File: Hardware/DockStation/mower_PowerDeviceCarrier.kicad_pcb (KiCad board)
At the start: 2 copper layers, 135.1 x 68.4 mm, 7 parts, among them J1 Conn_01x04, J2 Conn_01x04

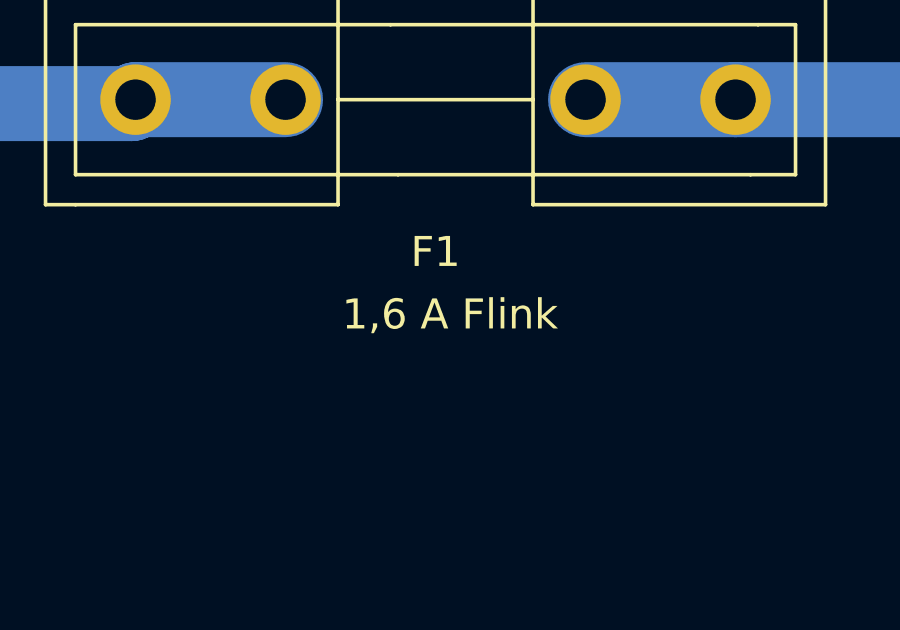
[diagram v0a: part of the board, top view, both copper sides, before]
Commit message: chore(dock): de translations
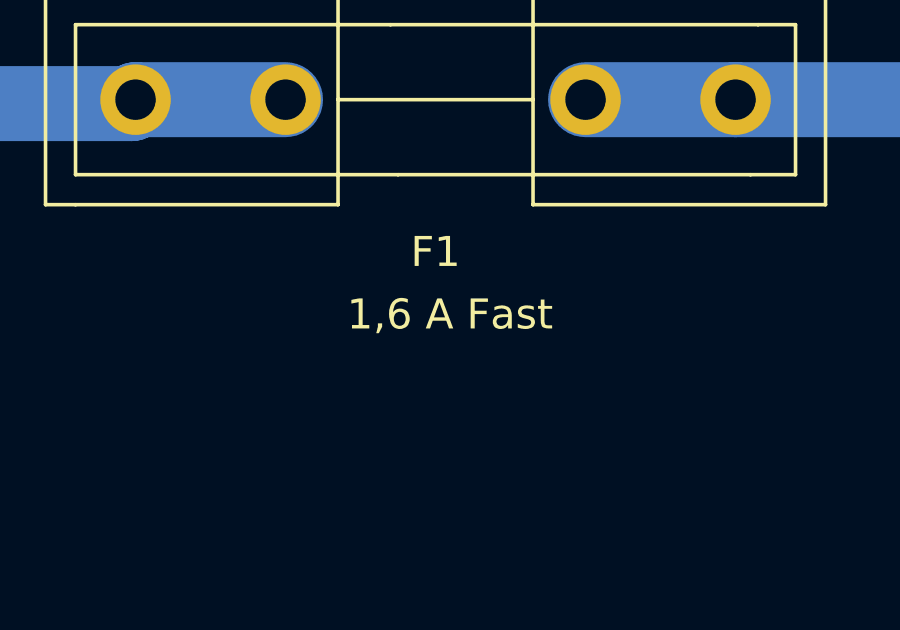
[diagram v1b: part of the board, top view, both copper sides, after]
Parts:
- A1: value DC-DC-Wandler -> DC-DC-Converter
- F1: value 1,6 A Flink -> 1,6 A Fast
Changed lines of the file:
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@@
       (effects (font (size 1 1) (thickness 0.15)))
     )
-    (fp_text value "1,6 A Flink" (at 9.5178 -7.1628) (layer "F.SilkS")
+    (fp_text value "1,6 A Fast" (at 9.5178 -7.1628) (layer "F.SilkS")
       (effects (font (size 1 1) (thickness 0.15)))
     )
@@
       (effects (font (size 1 1) (thickness 0.15)))
     )
-    (fp_text value "DC-DC-Wandler" (at 13.57 -1.76) (layer "F.Fab")
+    (fp_text value "DC-DC-Converter" (at 13.57 -1.76) (layer "F.Fab")
       (effects (font (size 1 1) (thickness 0.15)))
     )

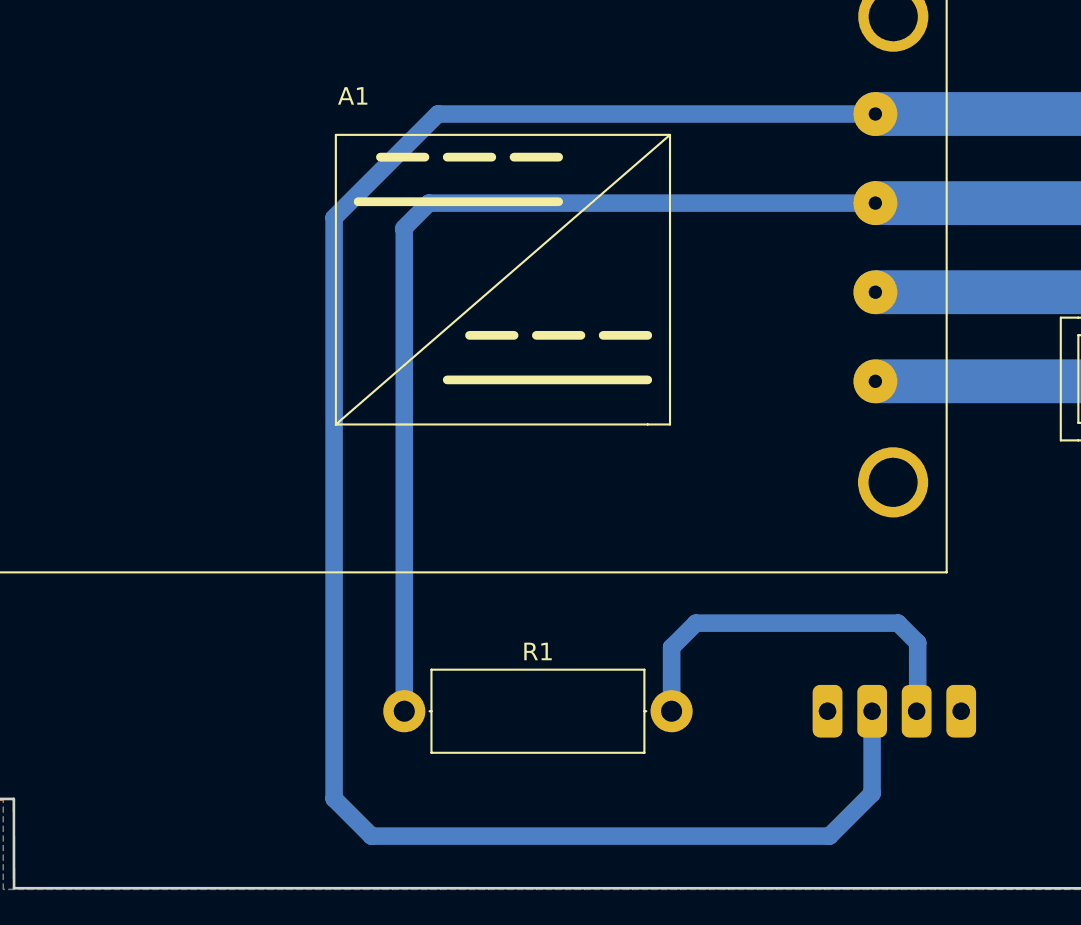
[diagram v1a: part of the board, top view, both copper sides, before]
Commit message: fix(dock): move led pin header to avoid screw hole overlap
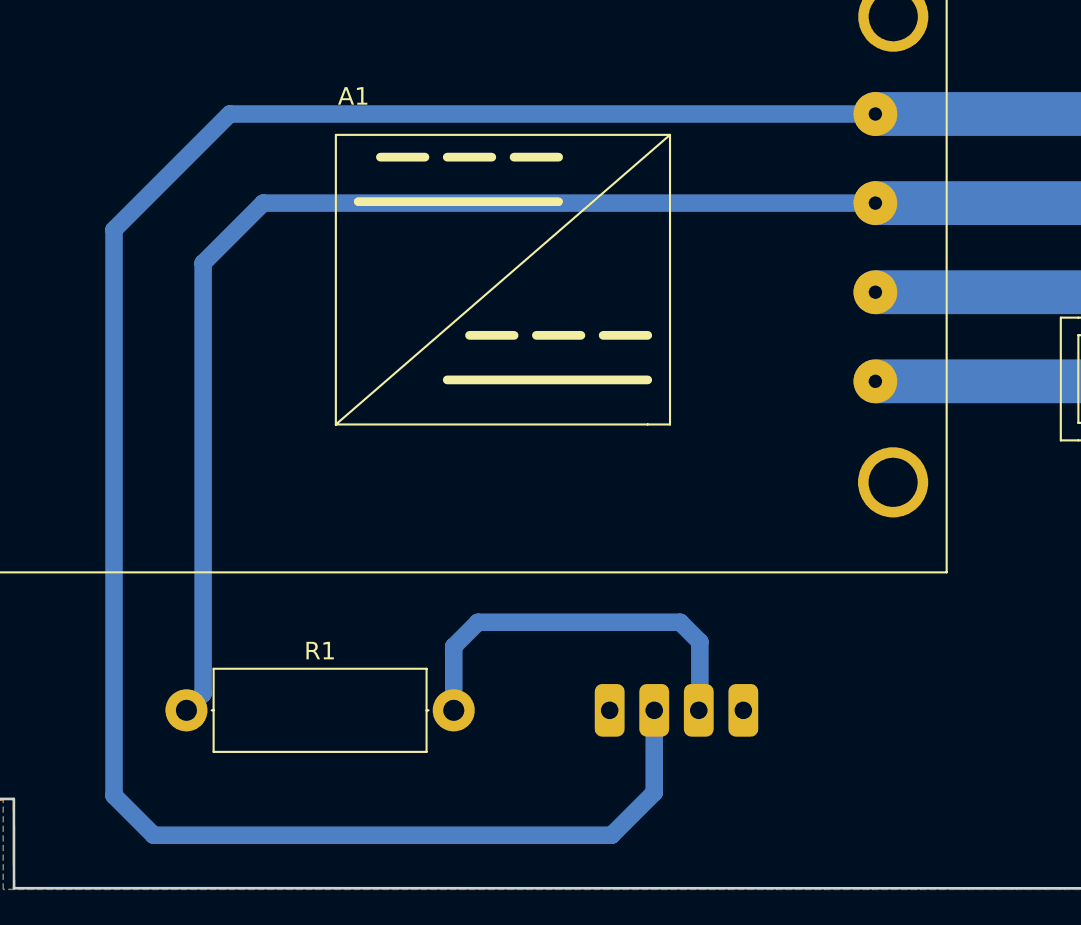
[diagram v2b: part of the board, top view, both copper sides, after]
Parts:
- moved R1 12.4 mm to (61.0, 109.3)
- moved J2 12.4 mm to (92.8, 109.3)
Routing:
- net +BATT: track 150.8 -> 162.9 mm
- net GND1: track 102.0 -> 112.7 mm
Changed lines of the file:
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@@
   )
   (footprint "Resistor_THT:R_Axial_DIN0414_L11.9mm_D4.5mm_P15.24mm_Horizontal" (layer "F.Cu")
-    (at 73.44 109.36)
+    (at 61.0194 109.3092)
     (descr "Resistor, Axial_DIN0414 series, Axial, Horizontal, pin pitch=15.24mm, 2W, length*diameter=11.9*4.5mm^2, http://www.vishay.com/docs/20128/wkxwrx.pdf")
     (tags "Resistor Axial_DIN0414 series Axial Horizontal pin pitch 15.24mm 2W length 11.9mm diameter 4.5mm")
@@
   )
   (footprint "ene9ba_footprint:PinHeader_1x04_P2.54mm_Horizontal" (layer "B.Cu")
-    (at 105.19 109.36 90)
+    (at 92.7694 109.3092 90)
     (descr "Through hole angled pin header, 1x04, 2.54mm pitch, 6mm pin length, single row")
     (tags "Through hole angled pin header THT 1x04 2.54mm single row")
@@
     (effects (font (size 1.5 1.5) (thickness 0.2)))
   )
-  (segment (start 74.844 80.3908) (end 73.4 81.8348) (width 1) (layer "B.Cu") (net 1))
-  (segment (start 100.2992 80.3908) (end 74.844 80.3908) (width 1) (layer "B.Cu") (net 1))
+  (segment (start 61.97 83.816) (end 65.3952 80.3908) (width 1) (layer "B.Cu") (net 1))
+  (segment (start 61.97 108.3586) (end 61.97 83.816) (width 1) (layer "B.Cu") (net 1))
   (segment (start 147.3427 80.3908) (end 147.3535 80.4016) (width 1) (layer "B.Cu") (net 1))
+  (segment (start 65.3952 80.3908) (end 100.2992 80.3908) (width 1) (layer "B.Cu") (net 1))
+  (segment (start 61.0194 109.3092) (end 61.97 108.3586) (width 1) (layer "B.Cu") (net 1))
   (segment (start 100.2992 80.3908) (end 147.3427 80.3908) (width 2.5) (layer "B.Cu") (net 1))
-  (segment (start 73.44 81.8748) (end 73.44 109.36) (width 1) (layer "B.Cu") (net 1))
+  (segment (start 85.2618 116.4296) (end 59.1506 116.4296) (width 1) (layer "B.Cu") (net 2))
+  (segment (start 87.6894 109.3092) (end 87.6894 114.002) (width 1) (layer "B.Cu") (net 2))
   (segment (start 100.2992 75.3108) (end 147.2627 75.3108) (width 2.5) (layer "B.Cu") (net 2))
-  (segment (start 100.11 109.36) (end 100.11 114.0528) (width 1) (layer "B.Cu") (net 2))
-  (segment (start 100.11 114.0528) (end 97.6824 116.4804) (width 1) (layer "B.Cu") (net 2))
-  (segment (start 69.4376 114.3468) (end 69.4376 81.2252) (width 1) (layer "B.Cu") (net 2))
-  (segment (start 97.6824 116.4804) (end 71.5712 116.4804) (width 1) (layer "B.Cu") (net 2))
+  (segment (start 87.6894 114.002) (end 85.2618 116.4296) (width 1) (layer "B.Cu") (net 2))
+  (segment (start 59.1506 116.4296) (end 56.89 114.169) (width 1) (layer "B.Cu") (net 2))
+  (segment (start 56.89 81.911) (end 63.4902 75.3108) (width 1) (layer "B.Cu") (net 2))
   (segment (start 147.2627 75.3108) (end 147.3535 75.4016) (width 1) (layer "B.Cu") (net 2))
-  (segment (start 75.352 75.3108) (end 100.2992 75.3108) (width 1) (layer "B.Cu") (net 2))
-  (segment (start 69.4376 81.2252) (end 75.352 75.3108) (width 1) (layer "B.Cu") (net 2))
-  (segment (start 71.5712 116.4804) (end 69.4376 114.3468) (width 1) (layer "B.Cu") (net 2))
+  (segment (start 63.4902 75.3108) (end 100.2992 75.3108) (width 1) (layer "B.Cu") (net 2))
+  (segment (start 56.89 114.169) (end 56.89 81.911) (width 1) (layer "B.Cu") (net 2))
   (segment (start 128.8702 90.42) (end 133.8702 90.42) (width 2.5) (layer "B.Cu") (net 5))
   (segment (start 133.8702 90.42) (end 147.3351 90.42) (width 2.5) (layer "B.Cu") (net 5))
@@
   (segment (start 100.2992 90.5508) (end 113.7394 90.5508) (width 2.5) (layer "B.Cu") (net 6))
   (segment (start 100.2992 85.4708) (end 147.2843 85.4708) (width 2.5) (layer "B.Cu") (net 7))
-  (segment (start 102.7116 109.2984) (end 102.65 109.36) (width 1) (layer "B.Cu") (net 8))
-  (segment (start 101.594 104.3392) (end 102.7116 105.4568) (width 1) (layer "B.Cu") (net 8))
-  (segment (start 102.7116 105.4568) (end 102.7116 109.2984) (width 1) (layer "B.Cu") (net 8))
-  (segment (start 88.68 109.36) (end 88.68 105.7216) (width 1) (layer "B.Cu") (net 8))
-  (segment (start 88.68 105.7216) (end 90.0624 104.3392) (width 1) (layer "B.Cu") (net 8))
-  (segment (start 90.0624 104.3392) (end 101.594 104.3392) (width 1) (layer "B.Cu") (net 8))
+  (segment (start 90.291 109.2476) (end 90.2294 109.3092) (width 1) (layer "B.Cu") (net 8))
+  (segment (start 89.1734 104.2884) (end 90.291 105.406) (width 1) (layer "B.Cu") (net 8))
+  (segment (start 90.291 105.406) (end 90.291 109.2476) (width 1) (layer "B.Cu") (net 8))
+  (segment (start 76.2594 109.3092) (end 76.2594 105.6708) (width 1) (layer "B.Cu") (net 8))
+  (segment (start 76.2594 105.6708) (end 77.6418 104.2884) (width 1) (layer "B.Cu") (net 8))
+  (segment (start 77.6418 104.2884) (end 89.1734 104.2884) (width 1) (layer "B.Cu") (net 8))
   (zone (net 7) (net_name "Net-(A1-Pad2)") (layers F&B.Cu) (hatch edge 0.508)
     (connect_pads (clearance 0.508))

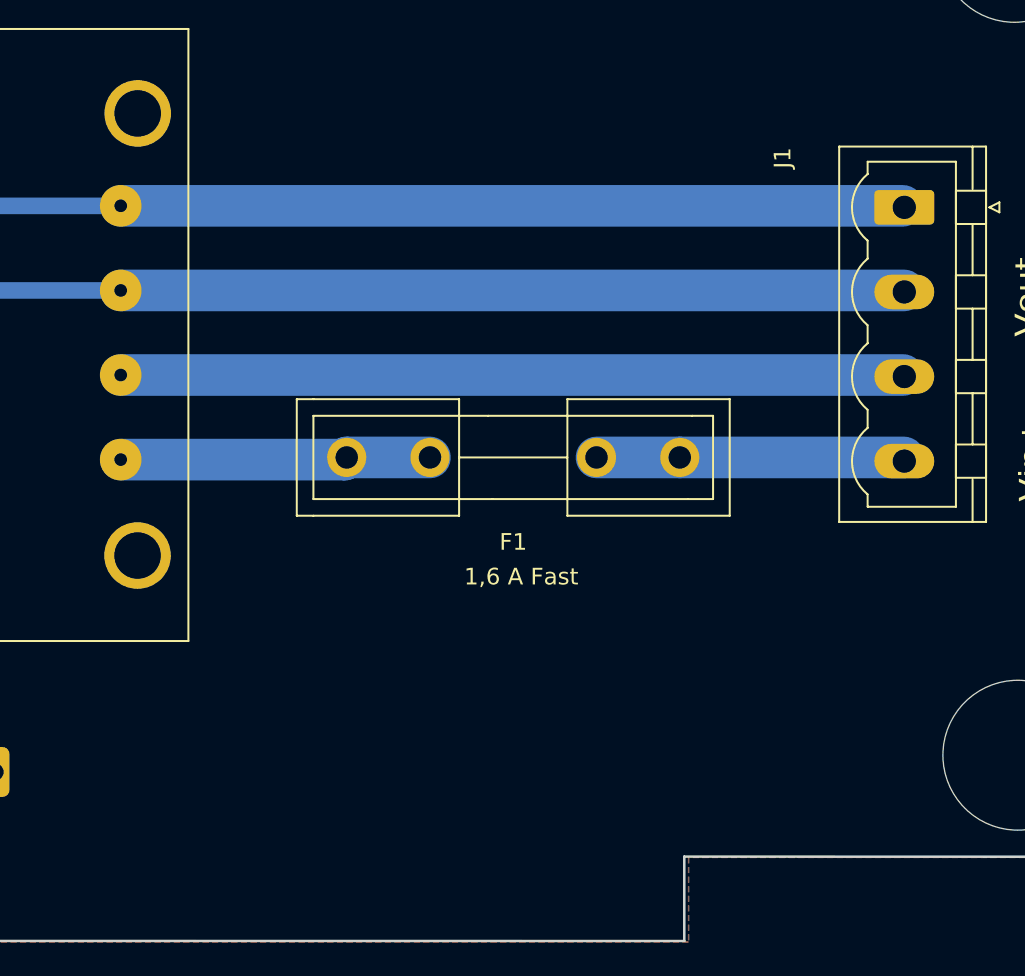
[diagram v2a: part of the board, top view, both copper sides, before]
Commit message: feat(dock): add 3.81mm terminals and pinholes to connect to dc/dc terminal
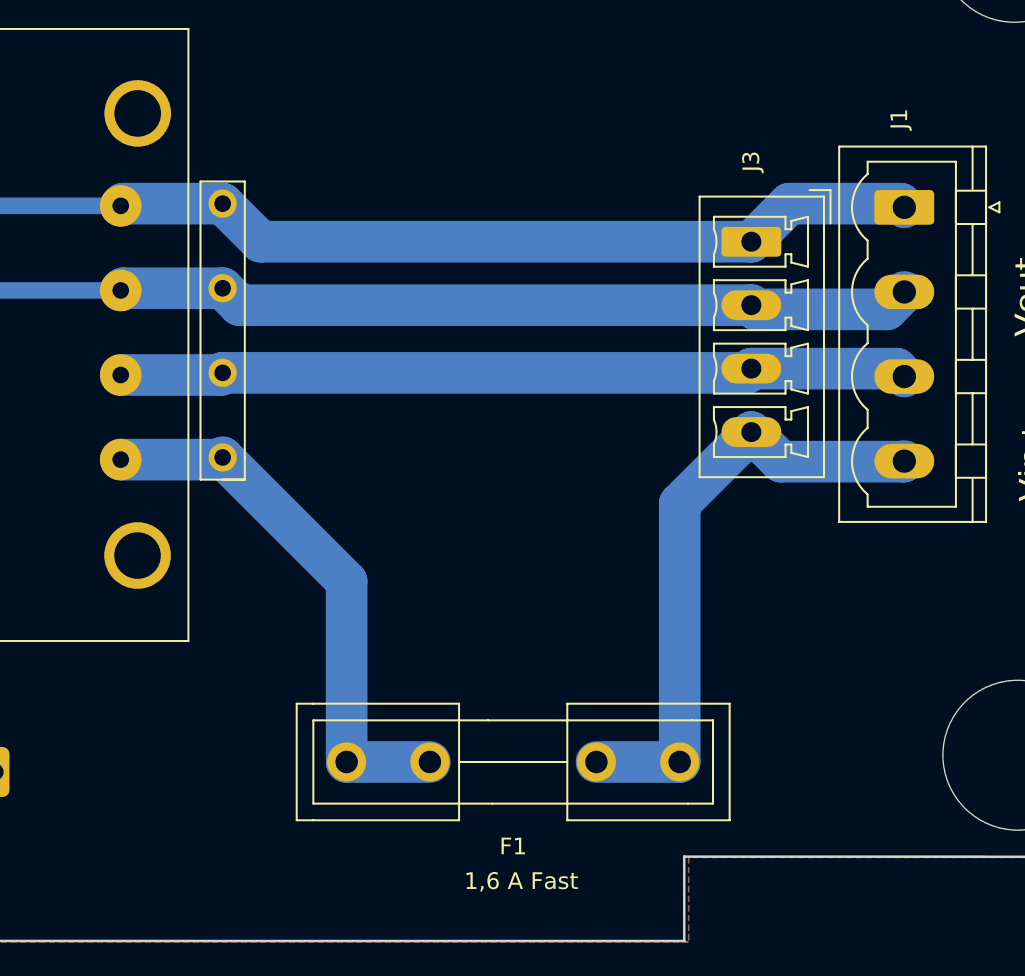
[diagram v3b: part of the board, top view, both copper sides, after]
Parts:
- removed REF**: ESD-Logo_6.6x6mm_SilkScreen, Symbol:ESD-Logo_6.6x6mm_SilkScreen
- added J3: Conn_01x04, Connector_Phoenix_MC:PhoenixContact_MCV_1,5_4-G-3.81_1x04_P3.81mm_Vertical, F.Cu at (138.2, 77.5)
- added J4: Conn_01x04, Connector_PinHeader_2.54mm:PinHeader_1x07_P2.54mm_Vertical, F.Cu at (106.4, 90.4)
- moved F1 18.3 mm to (133.9, 108.7)
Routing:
- net Net-(F1-Pad1): track 18.5 -> 36.5 mm
- net Net-(A1-Pad1): track 18.6 -> 32.5 mm
- net +BATT: track 162.9 -> 165.1 mm
- net GND1: track 112.7 -> 113.7 mm

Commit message: fix(dock): erc/drc
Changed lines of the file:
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@@
     (effects (font (size 1.5 1.5) (thickness 0.2)))
   )
+  (segment (start 147.3535 80.4816) (end 146.3051 81.53) (width 2.5) (layer "B.Cu") (net 1))
+  (segment (start 146.3051 81.53) (end 138.424 81.53) (width 2.5) (layer "B.Cu") (net 1))
   (segment (start 138.17 81.276) (end 107.436 81.276) (width 2.5) (layer "B.Cu") (net 1))
   (segment (start 138.17 81.276) (end 138.424 81.53) (width 2.5) (layer "B.Cu") (net 1))
   (segment (start 61.97 83.816) (end 65.3952 80.3908) (width 1) (layer "B.Cu") (net 1))
   (segment (start 61.97 108.3586) (end 61.97 83.816) (width 1) (layer "B.Cu") (net 1))
-  (segment (start 147.3427 80.3908) (end 147.3535 80.4016) (width 1) (layer "B.Cu") (net 1))
   (segment (start 106.42 80.26) (end 100.43 80.26) (width 2.5) (layer "B.Cu") (net 1))
-  (segment (start 138.424 81.53) (end 146.3051 81.53) (width 2.5) (layer "B.Cu") (net 1))
   (segment (start 65.3952 80.3908) (end 100.2992 80.3908) (width 1) (layer "B.Cu") (net 1))
   (segment (start 107.436 81.276) (end 106.42 80.26) (width 2.5) (layer "B.Cu") (net 1))
   (segment (start 61.0194 109.3092) (end 61.97 108.3586) (width 1) (layer "B.Cu") (net 1))
   (segment (start 100.43 80.26) (end 100.2992 80.3908) (width 2.5) (layer "B.Cu") (net 1))
-  (segment (start 146.3051 81.53) (end 147.3535 80.4816) (width 2.5) (layer "B.Cu") (net 1))
   (segment (start 85.2618 116.4296) (end 59.1506 116.4296) (width 1) (layer "B.Cu") (net 2))
   (segment (start 87.6894 109.3092) (end 87.6894 114.002) (width 1) (layer "B.Cu") (net 2))
@@
   (segment (start 100.43 75.18) (end 100.2992 75.3108) (width 2.5) (layer "B.Cu") (net 2))
   (segment (start 108.706 77.466) (end 106.42 75.18) (width 2.5) (layer "B.Cu") (net 2))
-  (segment (start 147.2627 75.3108) (end 147.3535 75.4016) (width 1) (layer "B.Cu") (net 2))
   (segment (start 63.4902 75.3108) (end 100.2992 75.3108) (width 1) (layer "B.Cu") (net 2))
   (segment (start 106.42 75.18) (end 100.43 75.18) (width 2.5) (layer "B.Cu") (net 2))
@@
   (segment (start 106.42 85.34) (end 137.916 85.34) (width 2.5) (layer "B.Cu") (net 7))
   (segment (start 106.2892 85.4708) (end 106.42 85.34) (width 2.5) (layer "B.Cu") (net 7))
-  (segment (start 90.291 109.2476) (end 90.2294 109.3092) (width 1) (layer "B.Cu") (net 8))
   (segment (start 89.1734 104.2884) (end 90.291 105.406) (width 1) (layer "B.Cu") (net 8))
   (segment (start 90.291 105.406) (end 90.291 109.2476) (width 1) (layer "B.Cu") (net 8))
